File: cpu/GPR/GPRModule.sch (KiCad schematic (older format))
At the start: 51 parts, among them J1 Interconnect, U1 74HCT574, U10 74LS245, U11 74LS125, U2 74HCT574, U3 74LS245, U4 74LS245, U5 74LS245, U6 74LS245, U7 74LS245, U8 74LS245, U9 74LS245

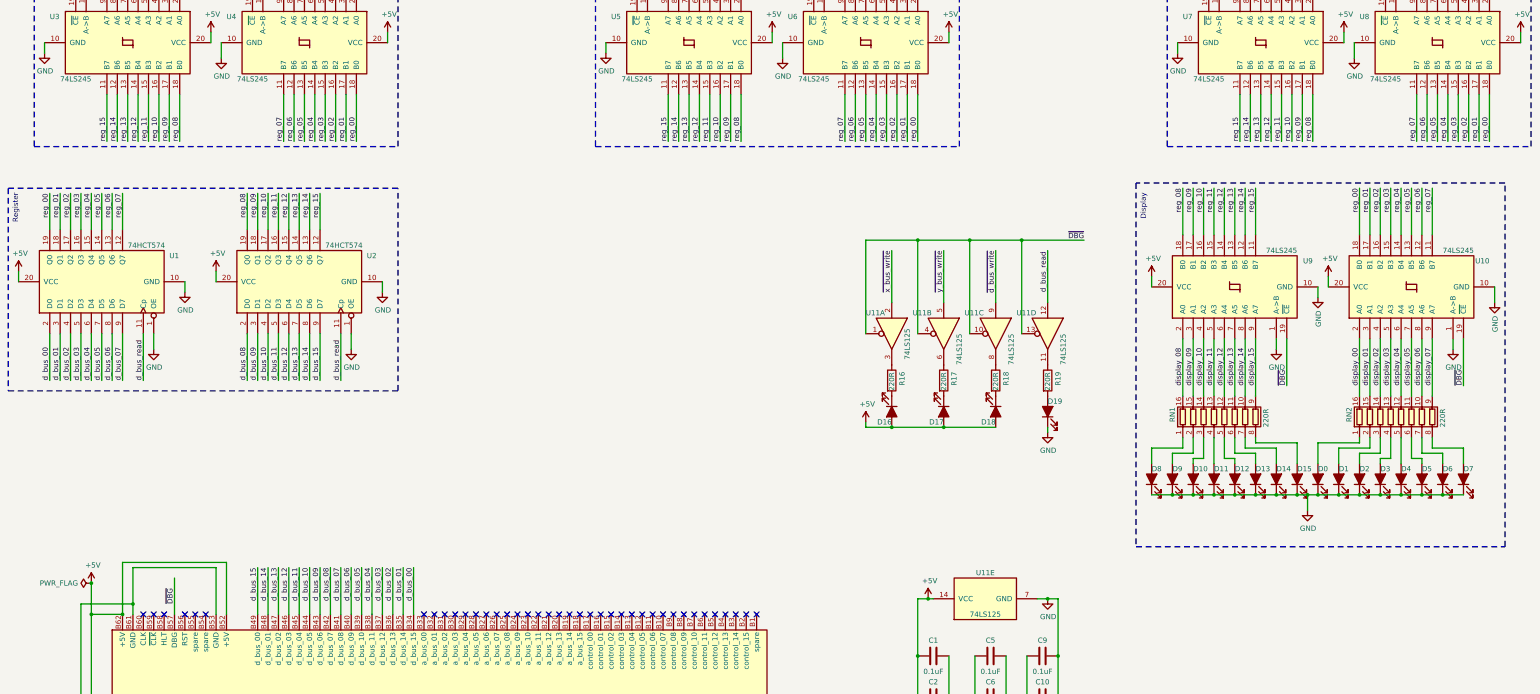
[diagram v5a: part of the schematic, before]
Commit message: V1.3 of GPR (fixed issues from first production board)
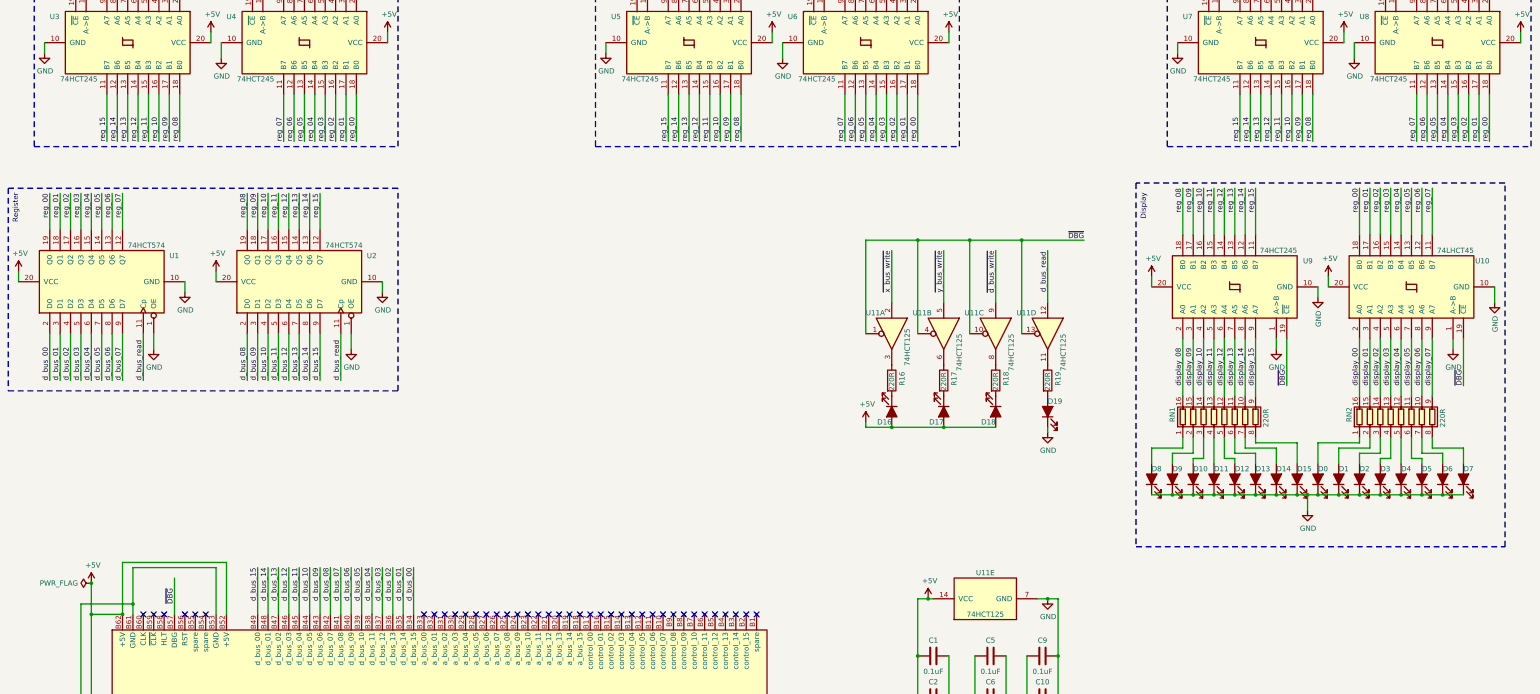
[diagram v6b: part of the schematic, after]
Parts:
- U10: value 74LS245 -> 74LHCT45
- U11: value 74LS125 -> 74HCT125
- U3, U4, U5, U6, U7, U8, U9: value 74LS245 -> 74HCT245
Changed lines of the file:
@@
 P 14850 4500
 F 0 "U10" V 15100 3750 50  0000 L CNN
-F 1 "74LS245" V 15200 3900 50  0000 L CNN
+F 1 "74LHCT45" V 15200 3900 50  0000 L CNN
 F 2 "Package_SO:SOIC-20W_7.5x12.8mm_P1.27mm" H 14850 4500 50  0001 C CNN
 F 3 "" H 14850 4500 50  0001 C CNN
@@
 P 2500 2150
 F 0 "U3" V 2250 1400 50  0000 L CNN
-F 1 "74LS245" V 2850 1500 50  0000 L CNN
+F 1 "74HCT245" V 2850 1500 50  0000 L CNN
 F 2 "Package_SO:SOIC-20W_7.5x12.8mm_P1.27mm" H 2500 2150 50  0001 C CNN
 F 3 "" H 2500 2150 50  0001 C CNN
@@
 P 4200 2150
 F 0 "U4" V 3950 1400 50  0000 L CNN
-F 1 "74LS245" V 4550 1500 50  0000 L CNN
+F 1 "74HCT245" V 4550 1500 50  0000 L CNN
 F 2 "Package_SO:SOIC-20W_7.5x12.8mm_P1.27mm" H 4200 2150 50  0001 C CNN
 F 3 "" H 4200 2150 50  0001 C CNN
@@
 P 7900 2150
 F 0 "U5" V 7650 1400 50  0000 L CNN
-F 1 "74LS245" V 8250 1500 50  0000 L CNN
+F 1 "74HCT245" V 8250 1500 50  0000 L CNN
 F 2 "Package_SO:SOIC-20W_7.5x12.8mm_P1.27mm" H 7900 2150 50  0001 C CNN
 F 3 "" H 7900 2150 50  0001 C CNN
@@
 P 9600 2150
 F 0 "U6" V 9350 1400 50  0000 L CNN
-F 1 "74LS245" V 9950 1500 50  0000 L CNN
+F 1 "74HCT245" V 9950 1500 50  0000 L CNN
 F 2 "Package_SO:SOIC-20W_7.5x12.8mm_P1.27mm" H 9600 2150 50  0001 C CNN
 F 3 "" H 9600 2150 50  0001 C CNN
@@
 P 13400 2150
 F 0 "U7" V 13150 1400 50  0000 L CNN
-F 1 "74LS245" V 13750 1500 50  0000 L CNN
+F 1 "74HCT245" V 13750 1500 50  0000 L CNN
 F 2 "Package_SO:SOIC-20W_7.5x12.8mm_P1.27mm" H 13400 2150 50  0001 C CNN
 F 3 "" H 13400 2150 50  0001 C CNN
@@
 P 15100 2150
 F 0 "U8" V 14850 1400 50  0000 L CNN
-F 1 "74LS245" V 15450 1500 50  0000 L CNN
+F 1 "74HCT245" V 15450 1500 50  0000 L CNN
 F 2 "Package_SO:SOIC-20W_7.5x12.8mm_P1.27mm" H 15100 2150 50  0001 C CNN
 F 3 "" H 15100 2150 50  0001 C CNN
@@
 P 13150 4500
 F 0 "U9" V 13400 3750 50  0000 L CNN
-F 1 "74LS245" V 13500 3900 50  0000 L CNN
+F 1 "74HCT245" V 13500 3900 50  0000 L CNN
 F 2 "Package_SO:SOIC-20W_7.5x12.8mm_P1.27mm" H 13150 4500 50  0001 C CNN
 F 3 "" H 13150 4500 50  0001 C CNN
@@
 P 9850 4950
 F 0 "U11" V 9650 4700 50  0000 L CNN
-F 1 "74LS125" H 9800 5100 50  0000 L CNN
+F 1 "74HCT125" H 9800 5100 50  0000 L CNN
 F 2 "Package_SO:SOIC-14_3.9x8.7mm_P1.27mm" H 9850 4950 50  0001 C CNN
 F 3 "http://www.ti.com/lit/gpn/sn74LS125" H 9850 4950 50  0001 C CNN
@@
 P 10350 4950
 F 0 "U11" V 10150 4650 50  0000 L CNN
-F 1 "74LS125" H 10350 5100 50  0000 L CNN
+F 1 "74HCT125" H 10350 5100 50  0000 L CNN
 F 2 "Package_SO:SOIC-14_3.9x8.7mm_P1.27mm" H 10350 4950 50  0001 C CNN
 F 3 "http://www.ti.com/lit/gpn/sn74LS125" H 10350 4950 50  0001 C CNN
@@
 P 10850 4950
 F 0 "U11" V 10650 4650 50  0000 L CNN
-F 1 "74LS125" H 10850 5100 50  0000 L CNN
+F 1 "74HCT125" H 10850 5100 50  0000 L CNN
 F 2 "Package_SO:SOIC-14_3.9x8.7mm_P1.27mm" H 10850 4950 50  0001 C CNN
 F 3 "http://www.ti.com/lit/gpn/sn74LS125" H 10850 4950 50  0001 C CNN
@@
 P 11350 4950
 F 0 "U11" V 11150 4650 50  0000 L CNN
-F 1 "74LS125" H 11350 5100 50  0000 L CNN
+F 1 "74HCT125" H 11350 5100 50  0000 L CNN
 F 2 "Package_SO:SOIC-14_3.9x8.7mm_P1.27mm" H 11350 4950 50  0001 C CNN
 F 3 "http://www.ti.com/lit/gpn/sn74LS125" H 11350 4950 50  0001 C CNN
@@
 P 10750 7500
 F 0 "U11" V 11000 7500 50  0000 C CNN
-F 1 "74LS125" V 10600 7500 50  0000 C CNN
+F 1 "74HCT125" V 10600 7500 50  0000 C CNN
 F 2 "Package_SO:SOIC-14_3.9x8.7mm_P1.27mm" H 10750 7500 50  0001 C CNN
 F 3 "http://www.ti.com/lit/gpn/sn74LS125" H 10750 7500 50  0001 C CNN

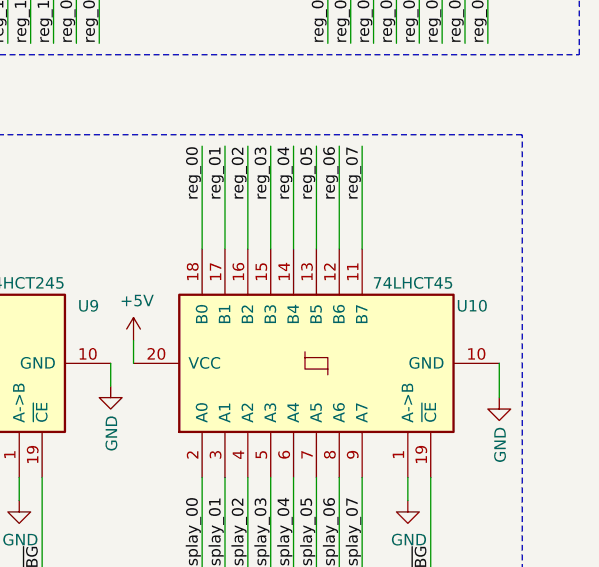
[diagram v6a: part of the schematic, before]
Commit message: Finished Address Register 1.0
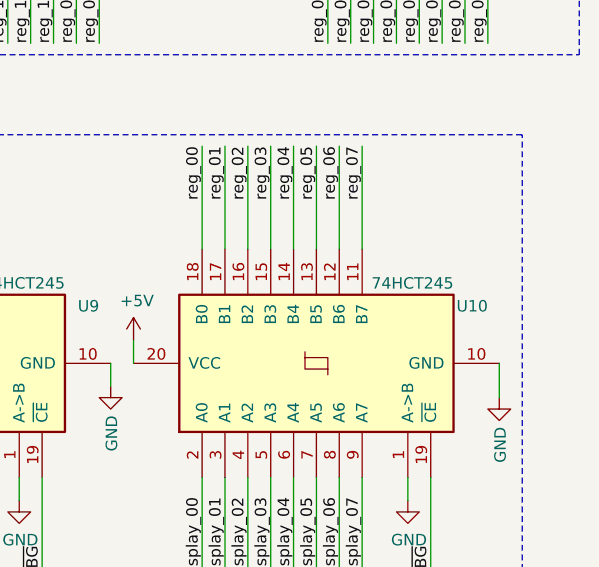
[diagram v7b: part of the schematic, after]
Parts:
- C12, C13: Digikey (none) -> 493-9786-1-ND
- D0, D1, D10, D11, D12, D13, D14, D15, D2, D3, D4, D5, D6, D7, D8, D9: Digikey 732-4978-1-ND -> 732-4991-1-ND
- D16, D17, D18, D19: Digikey 732-4988-1-ND -> 732-4994-1-ND
- RN1, RN2: Digikey (none) -> Y1221CT-ND
- U1, U2: Digikey (none) -> 296-14871-1-ND
- U10: value 74LHCT45 -> 74HCT245; Digikey (none) -> 296-1208-1-ND
- U11: Digikey (none) -> 296-14546-1-ND
- U3, U4, U5, U6, U7, U8, U9: Digikey (none) -> 296-1208-1-ND
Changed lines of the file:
@@
 F 2 "LED_SMD:LED_1206_3216Metric_Pad1.42x1.75mm_HandSolder" H 10350 5700 50  0001 C CNN
 F 3 "~" H 10350 5700 50  0001 C CNN
-F 4 "732-4988-1-ND" H 10350 5700 50  0001 C CNN "Digikey"
+F 4 "732-4994-1-ND" H 10350 5700 50  0001 C CNN "Digikey"
 	1    10350 5700
 	0    1    1    0
@@
 F 2 "LED_SMD:LED_1206_3216Metric_Pad1.42x1.75mm_HandSolder" H 10850 5700 50  0001 C CNN
 F 3 "~" H 10850 5700 50  0001 C CNN
-F 4 "732-4988-1-ND" H 10850 5700 50  0001 C CNN "Digikey"
+F 4 "732-4994-1-ND" H 10850 5700 50  0001 C CNN "Digikey"
 	1    10850 5700
 	0    1    1    0
@@
 F 2 "LED_SMD:LED_1206_3216Metric_Pad1.42x1.75mm_HandSolder" H 11350 5700 50  0001 C CNN
 F 3 "~" H 11350 5700 50  0001 C CNN
-F 4 "732-4988-1-ND" H 11350 5700 50  0001 C CNN "Digikey"
+F 4 "732-4994-1-ND" H 11350 5700 50  0001 C CNN "Digikey"
 	1    11350 5700
 	0    -1   -1   0
@@
 F 2 "LED_SMD:LED_1206_3216Metric_Pad1.42x1.75mm_HandSolder" H 9850 5700 50  0001 C CNN
 F 3 "~" H 9850 5700 50  0001 C CNN
-F 4 "732-4988-1-ND" H 9850 5700 50  0001 C CNN "Digikey"
+F 4 "732-4994-1-ND" H 9850 5700 50  0001 C CNN "Digikey"
 	1    9850 5700
 	0    1    1    0
@@
 F 2 "LED_SMD:LED_1206_3216Metric_Pad1.42x1.75mm_HandSolder" H 14950 6350 50  0001 C CNN
 F 3 "~" H 14950 6350 50  0001 C CNN
-F 4 "732-4978-1-ND" H 14950 6350 50  0001 C CNN "Digikey"
+F 4 "732-4991-1-ND" H 14950 6350 50  0001 C CNN "Digikey"
 	1    14950 6350
 	0    -1   -1   0
@@
 F 2 "LED_SMD:LED_1206_3216Metric_Pad1.42x1.75mm_HandSolder" H 12350 6350 50  0001 C CNN
 F 3 "~" H 12350 6350 50  0001 C CNN
-F 4 "732-4978-1-ND" H 12350 6350 50  0001 C CNN "Digikey"
+F 4 "732-4991-1-ND" H 12350 6350 50  0001 C CNN "Digikey"
 	1    12350 6350
 	0    -1   -1   0
@@
 F 2 "LED_SMD:LED_1206_3216Metric_Pad1.42x1.75mm_HandSolder" H 15350 6350 50  0001 C CNN
 F 3 "~" H 15350 6350 50  0001 C CNN
-F 4 "732-4978-1-ND" H 15350 6350 50  0001 C CNN "Digikey"
+F 4 "732-4991-1-ND" H 15350 6350 50  0001 C CNN "Digikey"
 	1    15350 6350
 	0    -1   -1   0
@@
 F 2 "LED_SMD:LED_1206_3216Metric_Pad1.42x1.75mm_HandSolder" H 15150 6350 50  0001 C CNN
 F 3 "~" H 15150 6350 50  0001 C CNN
-F 4 "732-4978-1-ND" H 15150 6350 50  0001 C CNN "Digikey"
+F 4 "732-4991-1-ND" H 15150 6350 50  0001 C CNN "Digikey"
 	1    15150 6350
 	0    -1   -1   0
@@
 F 2 "LED_SMD:LED_1206_3216Metric_Pad1.42x1.75mm_HandSolder" H 14750 6350 50  0001 C CNN
 F 3 "~" H 14750 6350 50  0001 C CNN
-F 4 "732-4978-1-ND" H 14750 6350 50  0001 C CNN "Digikey"
+F 4 "732-4991-1-ND" H 14750 6350 50  0001 C CNN "Digikey"
 	1    14750 6350
 	0    -1   -1   0
@@
 F 2 "LED_SMD:LED_1206_3216Metric_Pad1.42x1.75mm_HandSolder" H 14550 6350 50  0001 C CNN
 F 3 "~" H 14550 6350 50  0001 C CNN
-F 4 "732-4978-1-ND" H 14550 6350 50  0001 C CNN "Digikey"
+F 4 "732-4991-1-ND" H 14550 6350 50  0001 C CNN "Digikey"
 	1    14550 6350
 	0    -1   -1   0
@@
 F 2 "LED_SMD:LED_1206_3216Metric_Pad1.42x1.75mm_HandSolder" H 14350 6350 50  0001 C CNN
 F 3 "~" H 14350 6350 50  0001 C CNN
-F 4 "732-4978-1-ND" H 14350 6350 50  0001 C CNN "Digikey"
+F 4 "732-4991-1-ND" H 14350 6350 50  0001 C CNN "Digikey"
 	1    14350 6350
 	0    -1   -1   0
@@
 F 2 "LED_SMD:LED_1206_3216Metric_Pad1.42x1.75mm_HandSolder" H 14150 6350 50  0001 C CNN
 F 3 "~" H 14150 6350 50  0001 C CNN
-F 4 "732-4978-1-ND" H 14150 6350 50  0001 C CNN "Digikey"
+F 4 "732-4991-1-ND" H 14150 6350 50  0001 C CNN "Digikey"
 	1    14150 6350
 	0    -1   -1   0
@@
 F 2 "LED_SMD:LED_1206_3216Metric_Pad1.42x1.75mm_HandSolder" H 13950 6350 50  0001 C CNN
 F 3 "~" H 13950 6350 50  0001 C CNN
-F 4 "732-4978-1-ND" H 13950 6350 50  0001 C CNN "Digikey"
+F 4 "732-4991-1-ND" H 13950 6350 50  0001 C CNN "Digikey"
 	1    13950 6350
 	0    -1   -1   0
@@
 F 2 "LED_SMD:LED_1206_3216Metric_Pad1.42x1.75mm_HandSolder" H 13750 6350 50  0001 C CNN
 F 3 "~" H 13750 6350 50  0001 C CNN
-F 4 "732-4978-1-ND" H 13750 6350 50  0001 C CNN "Digikey"
+F 4 "732-4991-1-ND" H 13750 6350 50  0001 C CNN "Digikey"
 	1    13750 6350
 	0    -1   -1   0
@@
 F 2 "LED_SMD:LED_1206_3216Metric_Pad1.42x1.75mm_HandSolder" H 13550 6350 50  0001 C CNN
 F 3 "~" H 13550 6350 50  0001 C CNN
-F 4 "732-4978-1-ND" H 13550 6350 50  0001 C CNN "Digikey"
+F 4 "732-4991-1-ND" H 13550 6350 50  0001 C CNN "Digikey"
 	1    13550 6350
 	0    -1   -1   0
@@
 F 2 "LED_SMD:LED_1206_3216Metric_Pad1.42x1.75mm_HandSolder" H 13350 6350 50  0001 C CNN
 F 3 "~" H 13350 6350 50  0001 C CNN
-F 4 "732-4978-1-ND" H 13350 6350 50  0001 C CNN "Digikey"
+F 4 "732-4991-1-ND" H 13350 6350 50  0001 C CNN "Digikey"
 	1    13350 6350
 	0    -1   -1   0
@@
 F 2 "LED_SMD:LED_1206_3216Metric_Pad1.42x1.75mm_HandSolder" H 13150 6350 50  0001 C CNN
 F 3 "~" H 13150 6350 50  0001 C CNN
-F 4 "732-4978-1-ND" H 13150 6350 50  0001 C CNN "Digikey"
+F 4 "732-4991-1-ND" H 13150 6350 50  0001 C CNN "Digikey"
 	1    13150 6350
 	0    -1   -1   0
@@
 F 2 "LED_SMD:LED_1206_3216Metric_Pad1.42x1.75mm_HandSolder" H 12950 6350 50  0001 C CNN
 F 3 "~" H 12950 6350 50  0001 C CNN
-F 4 "732-4978-1-ND" H 12950 6350 50  0001 C CNN "Digikey"
+F 4 "732-4991-1-ND" H 12950 6350 50  0001 C CNN "Digikey"
 	1    12950 6350
 	0    -1   -1   0
@@
 F 2 "LED_SMD:LED_1206_3216Metric_Pad1.42x1.75mm_HandSolder" H 12750 6350 50  0001 C CNN
 F 3 "~" H 12750 6350 50  0001 C CNN
-F 4 "732-4978-1-ND" H 12750 6350 50  0001 C CNN "Digikey"
+F 4 "732-4991-1-ND" H 12750 6350 50  0001 C CNN "Digikey"
 	1    12750 6350
 	0    -1   -1   0
@@
 F 2 "LED_SMD:LED_1206_3216Metric_Pad1.42x1.75mm_HandSolder" H 12550 6350 50  0001 C CNN
 F 3 "~" H 12550 6350 50  0001 C CNN
-F 4 "732-4978-1-ND" H 12550 6350 50  0001 C CNN "Digikey"
+F 4 "732-4991-1-ND" H 12550 6350 50  0001 C CNN "Digikey"
 	1    12550 6350
 	0    -1   -1   0
@@
 F 2 "Package_SO:SOIC-20W_7.5x12.8mm_P1.27mm" H 2250 4450 50  0001 C CNN
 F 3 "http://www.ti.com/lit/gpn/sn74HCT574" H 2250 4450 50  0001 C CNN
+F 4 "296-14871-1-ND" H 2250 4450 50  0001 C CNN "Digikey"
 	1    2250 4450
 	0    -1   -1   0
@@
 F 2 "Package_SO:SOIC-20W_7.5x12.8mm_P1.27mm" H 4150 4450 50  0001 C CNN
 F 3 "http://www.ti.com/lit/gpn/sn74HCT574" H 4150 4450 50  0001 C CNN
+F 4 "296-14871-1-ND" H 4150 4450 50  0001 C CNN "Digikey"
 	1    4150 4450
 	0    -1   -1   0
@@
 P 14850 4500
 F 0 "U10" V 15100 3750 50  0000 L CNN
-F 1 "74LHCT45" V 15200 3900 50  0000 L CNN
+F 1 "74HCT245" V 15200 3900 50  0000 L CNN
 F 2 "Package_SO:SOIC-20W_7.5x12.8mm_P1.27mm" H 14850 4500 50  0001 C CNN
 F 3 "" H 14850 4500 50  0001 C CNN
+F 4 "296-1208-1-ND" H 14850 4500 50  0001 C CNN "Digikey"
 	1    14850 4500
 	0    -1   -1   0
@@
 F 2 "Package_SO:SOIC-20W_7.5x12.8mm_P1.27mm" H 2500 2150 50  0001 C CNN
 F 3 "" H 2500 2150 50  0001 C CNN
+F 4 "296-1208-1-ND" H 2500 2150 50  0001 C CNN "Digikey"
 	1    2500 2150
 	0    1    1    0
@@
 F 2 "Package_SO:SOIC-20W_7.5x12.8mm_P1.27mm" H 4200 2150 50  0001 C CNN
 F 3 "" H 4200 2150 50  0001 C CNN
+F 4 "296-1208-1-ND" H 4200 2150 50  0001 C CNN "Digikey"
 	1    4200 2150
 	0    1    1    0
@@
 F 2 "Package_SO:SOIC-20W_7.5x12.8mm_P1.27mm" H 7900 2150 50  0001 C CNN
 F 3 "" H 7900 2150 50  0001 C CNN
+F 4 "296-1208-1-ND" H 7900 2150 50  0001 C CNN "Digikey"
 	1    7900 2150
 	0    1    1    0
@@
 F 2 "Package_SO:SOIC-20W_7.5x12.8mm_P1.27mm" H 9600 2150 50  0001 C CNN
 F 3 "" H 9600 2150 50  0001 C CNN
+F 4 "296-1208-1-ND" H 9600 2150 50  0001 C CNN "Digikey"
 	1    9600 2150
 	0    1    1    0
@@
 F 2 "Package_SO:SOIC-20W_7.5x12.8mm_P1.27mm" H 13400 2150 50  0001 C CNN
 F 3 "" H 13400 2150 50  0001 C CNN
+F 4 "296-1208-1-ND" H 13400 2150 50  0001 C CNN "Digikey"
 	1    13400 2150
 	0    1    1    0
@@
 F 2 "Package_SO:SOIC-20W_7.5x12.8mm_P1.27mm" H 15100 2150 50  0001 C CNN
 F 3 "" H 15100 2150 50  0001 C CNN
+F 4 "296-1208-1-ND" H 15100 2150 50  0001 C CNN "Digikey"
 	1    15100 2150
 	0    1    1    0
@@
 F 2 "Package_SO:SOIC-20W_7.5x12.8mm_P1.27mm" H 13150 4500 50  0001 C CNN
 F 3 "" H 13150 4500 50  0001 C CNN
+F 4 "296-1208-1-ND" H 13150 4500 50  0001 C CNN "Digikey"
 	1    13150 4500
 	0    -1   -1   0
@@
 F 2 "Resistor_SMD:R_Array_Convex_8x0602" V 13525 5750 50  0001 C CNN
 F 3 "~" H 13050 5750 50  0001 C CNN
+F 4 "Y1221CT-ND" H 13050 5750 50  0001 C CNN "Digikey"
 	1    13050 5750
 	1    0    0    -1
@@
 F 2 "Resistor_SMD:R_Array_Convex_8x0602" V 15225 5750 50  0001 C CNN
 F 3 "~" H 14750 5750 50  0001 C CNN
+F 4 "Y1221CT-ND" H 14750 5750 50  0001 C CNN "Digikey"
 	1    14750 5750
 	1    0    0    -1
@@
 F 2 "Capacitor_SMD:CP_Elec_4x5.4" H 11300 9300 50  0001 C CNN
 F 3 "~" H 11300 9300 50  0001 C CNN
+F 4 "493-9786-1-ND" H 11300 9300 50  0001 C CNN "Digikey"
 	1    11300 9300
 	0    -1   -1   0
@@
 F 2 "Capacitor_SMD:CP_Elec_4x5.4" H 11300 9750 50  0001 C CNN
 F 3 "~" H 11300 9750 50  0001 C CNN
+F 4 "493-9786-1-ND" H 11300 9750 50  0001 C CNN "Digikey"
 	1    11300 9750
 	0    -1   -1   0
@@
 F 2 "Package_SO:SOIC-14_3.9x8.7mm_P1.27mm" H 9850 4950 50  0001 C CNN
 F 3 "http://www.ti.com/lit/gpn/sn74LS125" H 9850 4950 50  0001 C CNN
+F 4 "296-14546-1-ND" H 9850 4950 50  0001 C CNN "Digikey"
 	1    9850 4950
 	0    1    1    0
@@
 F 2 "Package_SO:SOIC-14_3.9x8.7mm_P1.27mm" H 10350 4950 50  0001 C CNN
 F 3 "http://www.ti.com/lit/gpn/sn74LS125" H 10350 4950 50  0001 C CNN
+F 4 "296-14546-1-ND" H 10350 4950 50  0001 C CNN "Digikey"
 	2    10350 4950
 	0    1    1    0
@@
 F 2 "Package_SO:SOIC-14_3.9x8.7mm_P1.27mm" H 10850 4950 50  0001 C CNN
 F 3 "http://www.ti.com/lit/gpn/sn74LS125" H 10850 4950 50  0001 C CNN
+F 4 "296-14546-1-ND" H 10850 4950 50  0001 C CNN "Digikey"
 	3    10850 4950
 	0    1    1    0
@@
 F 2 "Package_SO:SOIC-14_3.9x8.7mm_P1.27mm" H 11350 4950 50  0001 C CNN
 F 3 "http://www.ti.com/lit/gpn/sn74LS125" H 11350 4950 50  0001 C CNN
+F 4 "296-14546-1-ND" H 11350 4950 50  0001 C CNN "Digikey"
 	4    11350 4950
 	0    1    1    0
@@
 F 2 "Package_SO:SOIC-14_3.9x8.7mm_P1.27mm" H 10750 7500 50  0001 C CNN
 F 3 "http://www.ti.com/lit/gpn/sn74LS125" H 10750 7500 50  0001 C CNN
+F 4 "296-14546-1-ND" H 10750 7500 50  0001 C CNN "Digikey"
 	5    10750 7500
 	0    -1   -1   0
